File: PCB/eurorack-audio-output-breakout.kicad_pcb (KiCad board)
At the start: 2 copper layers, 18.4 x 50.5 mm, 12 parts, among them J1 Conn_01x04_Pin, J10 A, J11 B, J12 Conn_01x05_Pin, J3 Conn_01x04_Pin, J4 Conn_01x02_Pin, J5 Conn_01x05_Pin, U1 TL072

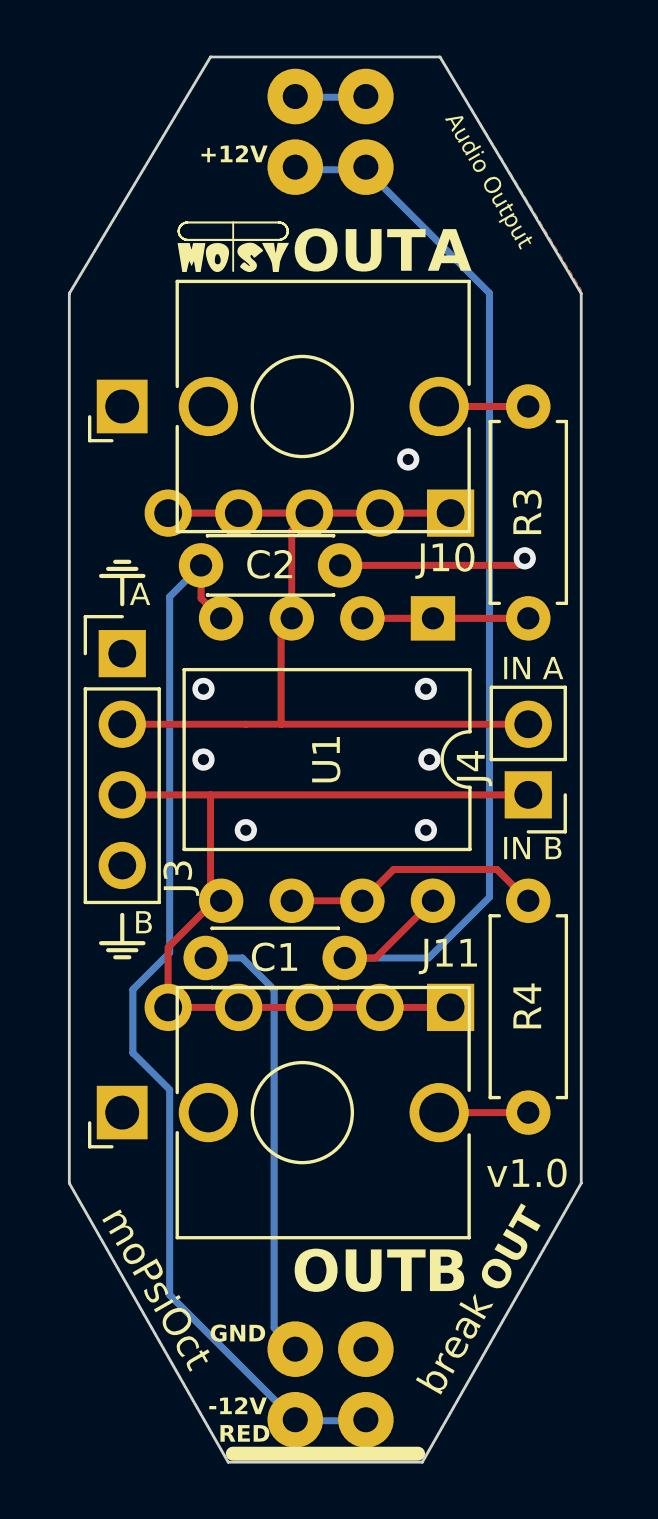
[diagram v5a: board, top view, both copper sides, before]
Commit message: Fix U1 footprint
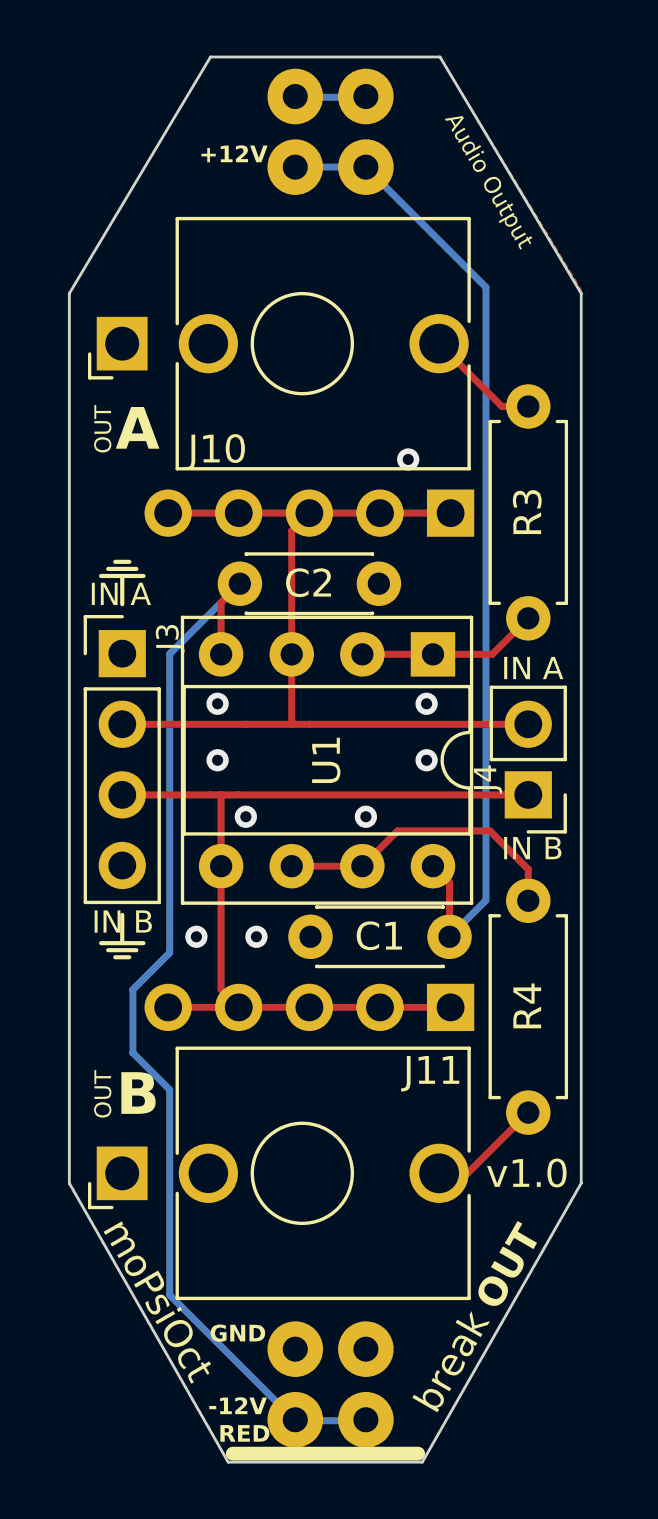
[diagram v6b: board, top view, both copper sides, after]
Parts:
- U1: footprint Package_DIP:DIP-8_W10.16mm -> Package_DIP:DIP-8_W7.62mm_Socket
- moved C1 3.85 mm to (195.5, 95.2)
- moved J10 2.26 mm to (190.2, 73.9)
- moved J11 2.18 mm to (190.2, 103.8)
- moved C2 1.55 mm to (193.0, 82.5)
- moved U1 1.30 mm to (194.9, 85.1)
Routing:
- net GND: track 23.0 -> 0.00 mm, vias 8 -> 9
- net +12V: track 40.7 -> 35.3 mm
- net Net-(U1B--): track 9.44 -> 10.7 mm
- net Net-(J10-PadT): track 3.21 -> 4.14 mm
- net Net-(J12-Pin_1): track 33.5 -> 32.7 mm
- net Net-(U1A--): track 5.97 -> 6.51 mm
- net -12V: track 39.0 -> 39.5 mm
